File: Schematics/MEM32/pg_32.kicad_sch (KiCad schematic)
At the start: 16 parts

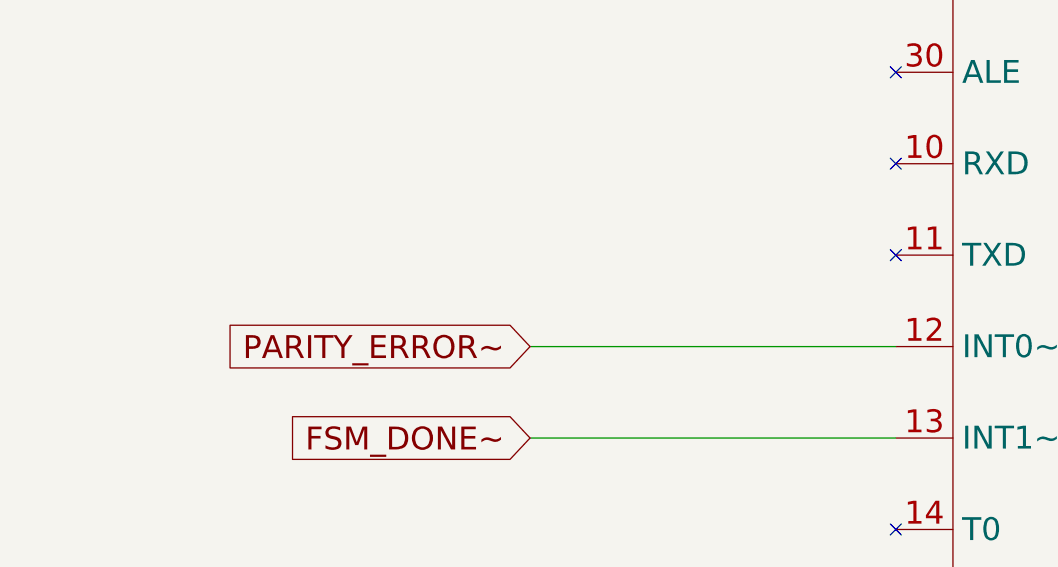
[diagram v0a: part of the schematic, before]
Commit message: MEM32: Disable parity check, good to 7.37s (rm096)
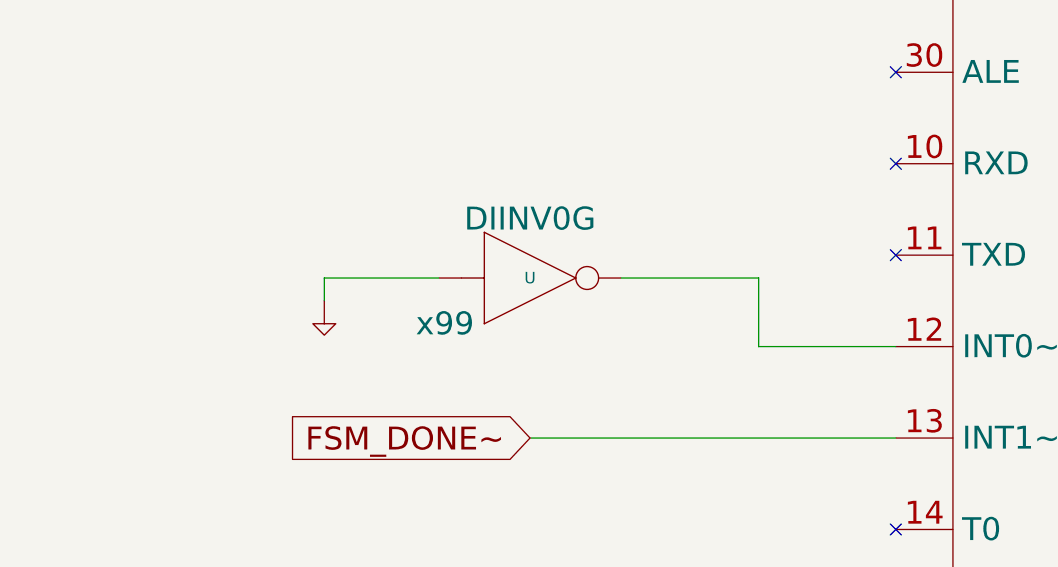
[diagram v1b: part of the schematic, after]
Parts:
- added U: (no value), symbol r1000:F04
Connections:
- net PD: now also U.1 (D0)
- net PARITY_ERROR~: no longer names the net of U.12 (INT0~)
- net PARITY_ERROR~: now also U.2 (Q)
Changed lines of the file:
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@@
-    (stroke (width 0) (type default))
-  )
-  (wire (pts (xy 88.9 137.16) (xy 129.54 137.16))
     (stroke (width 0) (type default))
   )
@@
     (stroke (width 0) (type default))
   )
+  (wire (pts (xy 66.04 129.54) (xy 78.74 129.54))
+    (stroke (width 0) (type default))
+  )
   (wire (pts (xy 289.56 243.84) (xy 289.56 248.92))
     (stroke (width 0) (type default))
@@
     (stroke (width 0) (type default))
   )
+  (wire (pts (xy 114.3 137.16) (xy 129.54 137.16))
+    (stroke (width 0) (type default))
+  )
   (wire (pts (xy 378.46 246.38) (xy 419.1 246.38))
     (stroke (width 0) (type default))
@@
     (stroke (width 0) (type default))
   )
+  (wire (pts (xy 114.3 129.54) (xy 114.3 137.16))
+    (stroke (width 0) (type default))
+  )
   (wire (pts (xy 289.56 233.68) (xy 292.1 233.68))
     (stroke (width 0) (type default))
@@
     (stroke (width 0) (type default))
   )
+  (wire (pts (xy 99.06 129.54) (xy 114.3 129.54))
+    (stroke (width 0) (type default))
+  )
   (wire (pts (xy 177.8 147.32) (xy 218.44 147.32))
     (stroke (width 0) (type default))
@@
     (stroke (width 0) (type default))
   )
+  (wire (pts (xy 66.04 132.08) (xy 66.04 129.54))
+    (stroke (width 0) (type default))
+  )
   (wire (pts (xy 523.24 160.02) (xy 535.94 160.02))
     (stroke (width 0) (type default))
@@
   (label "DIAG_4" (at 378.46 210.82 0) (fields_autoplaced)
     (effects (font (size 2.54 2.54)) (justify left bottom))
-  )
-  (global_label "PARITY_ERROR~" (shape input) (at 88.9 137.16 180) (fields_autoplaced)
-    (effects (font (size 2.54 2.54)) (justify right))
-    (property "Intersheet References" "${INTERSHEET_REFS}" (id 0) (at 55.3569 137.0013 0)
-      (effects (font (size 1.905 1.905)) (justify right))
-    )
   )
   (global_label "P_TO_S_SEL1" (shape input) (at 287.02 335.28 180) (fields_autoplaced)
@@
     (pin "2")
     (pin "3")
+  )
+  (symbol (lib_id "r1000:PD") (at 66.04 132.08 0) (unit 1)
+    (in_bom no) (on_board yes)
+    (default_instance (reference "U") (unit 1) (value "") (footprint ""))
+    (property "Reference" "U" (id 0) (at 66.04 132.08 0)
+      (effects (font (size 1.27 1.27)) hide)
+    )
+    (property "Value" "" (id 1) (at 66.04 132.08 0)
+      (effects (font (size 1.27 1.27)) hide)
+    )
+    (property "Footprint" "" (id 2) (at 66.04 132.08 0)
+      (effects (font (size 1.27 1.27)) hide)
+    )
+    (property "Datasheet" "" (id 3) (at 66.04 132.08 0)
+      (effects (font (size 1.27 1.27)) hide)
+    )
+    (pin "1")
   )
   (symbol (lib_id "r1000:F04") (at 513.08 160.02 0) (unit 1)
@@
     (pin "9")
   )
+  (symbol (lib_id "r1000:F04") (at 88.9 129.54 0) (unit 1)
+    (in_bom yes) (on_board yes)
+    (default_instance (reference "U") (unit 1) (value "") (footprint ""))
+    (property "Reference" "U" (id 0) (at 88.9 129.54 0)
+      (effects (font (size 1.27 1.27)))
+    )
+    (property "Value" "" (id 1) (at 90.17 134.62 0)
+      (effects (font (size 2.54 2.54)) (justify left))
+    )
+    (property "Footprint" "" (id 2) (at 88.9 129.54 0)
+      (effects (font (size 1.27 1.27)) hide)
+    )
+    (property "Datasheet" "" (id 3) (at 88.9 129.54 0)
+      (effects (font (size 1.27 1.27)) hide)
+    )
+    (property "Location" "x99" (id 4) (at 76.2 134.62 0)
+      (effects (font (size 2.54 2.54)) (justify left))
+    )
+    (property "Name" "DIINV0G" (id 5) (at 88.9 124.46 0)
+      (effects (font (size 2.54 2.54)) (justify bottom))
+    )
+    (pin "1")
+    (pin "2")
+  )
   (symbol (lib_id "r1000:NOVRAM") (at 213.36 350.52 0) (unit 1)

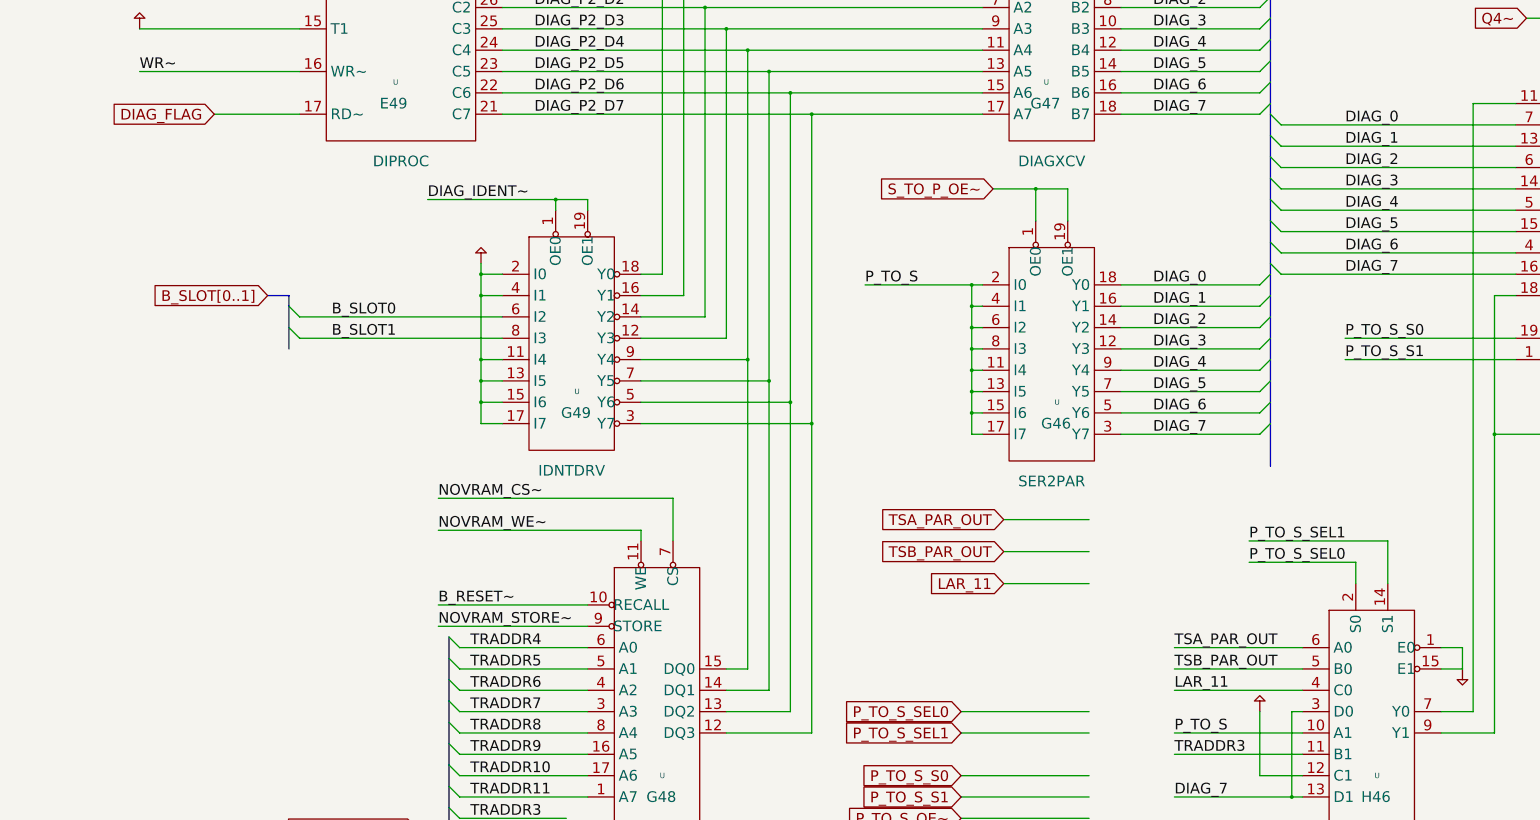
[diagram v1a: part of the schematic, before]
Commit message: DFSM pruning.  Tested to 13.72s
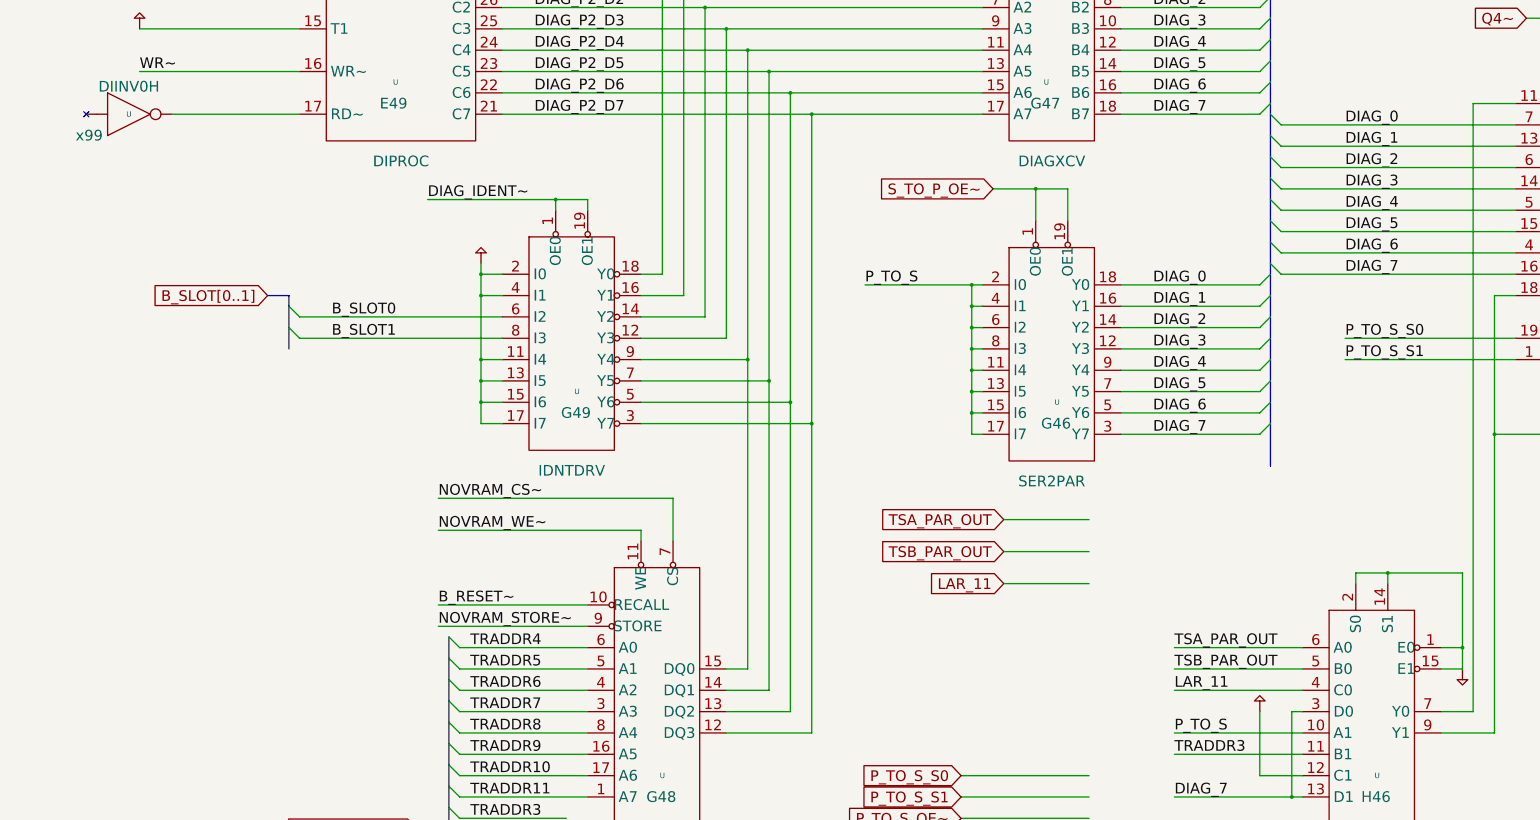
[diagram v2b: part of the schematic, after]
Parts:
- added U: (no value), symbol r1000:F04
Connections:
- net P_TO_S_SEL0 is gone; now on net PD: U.2 (S0)
- net P_TO_S_SEL1 is gone; now on net PD: U.14 (S1)
- net DIAG_FLAG: no longer names the net of U.17 (RD~)
- net DIAG_FLAG: now also U.2 (Q)
- no-connect marks 11 -> 12
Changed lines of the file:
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@@
   (junction (at 289.56 233.68) (diameter 0) (color 0 0 0 0)
   )
+  (junction (at 388.62 297.18) (diameter 0) (color 0 0 0 0)
+  )
   (junction (at 246.38 182.88) (diameter 0) (color 0 0 0 0)
   )
@@
   )
   (junction (at 289.56 254) (diameter 0) (color 0 0 0 0)
+  )
+  (junction (at 406.4 314.96) (diameter 0) (color 0 0 0 0)
   )
   (junction (at 289.56 248.92) (diameter 0) (color 0 0 0 0)
@@
   (no_connect (at 129.54 157.48))
   (no_connect (at 129.54 106.68))
+  (no_connect (at 78.74 187.96))
   (no_connect (at 129.54 116.84))
   (no_connect (at 129.54 127))
@@
     (stroke (width 0) (type default))
   )
-  (wire (pts (xy 355.6 294.64) (xy 381 294.64))
-    (stroke (width 0) (type default))
-  )
   (bus (pts (xy 294.64 83.82) (xy 294.64 88.9))
     (stroke (width 0) (type default))
@@
     (stroke (width 0) (type default))
   )
+  (wire (pts (xy 406.4 297.18) (xy 406.4 314.96))
+    (stroke (width 0) (type default))
+  )
   (wire (pts (xy 297.18 299.72) (xy 317.5 299.72))
     (stroke (width 0) (type default))
@@
     (stroke (width 0) (type default))
   )
+  (wire (pts (xy 381 297.18) (xy 388.62 297.18))
+    (stroke (width 0) (type default))
+  )
   (wire (pts (xy 325.12 233.68) (xy 358.14 233.68))
     (stroke (width 0) (type default))
@@
     (stroke (width 0) (type default))
   )
-  (wire (pts (xy 388.62 299.72) (xy 388.62 289.56))
-    (stroke (width 0) (type default))
-  )
   (wire (pts (xy 259.08 81.28) (xy 292.1 81.28))
     (stroke (width 0) (type default))
@@
     (stroke (width 0) (type default))
   )
-  (wire (pts (xy 287.02 335.28) (xy 317.5 335.28))
-    (stroke (width 0) (type default))
-  )
   (bus (pts (xy 360.68 203.2) (xy 360.68 208.28))
     (stroke (width 0) (type default))
@@
     (stroke (width 0) (type default))
   )
+  (wire (pts (xy 388.62 297.18) (xy 406.4 297.18))
+    (stroke (width 0) (type default))
+  )
   (wire (pts (xy 162.56 287.02) (xy 210.82 287.02))
     (stroke (width 0) (type default))
@@
     (stroke (width 0) (type default))
   )
+  (wire (pts (xy 388.62 299.72) (xy 388.62 297.18))
+    (stroke (width 0) (type default))
+  )
   (bus (pts (xy 360.68 226.06) (xy 360.68 231.14))
     (stroke (width 0) (type default))
   )
-  (wire (pts (xy 287.02 330.2) (xy 317.5 330.2))
-    (stroke (width 0) (type default))
-  )
   (wire (pts (xy 251.46 187.96) (xy 292.1 187.96))
     (stroke (width 0) (type default))
@@
     (stroke (width 0) (type default))
   )
+  (wire (pts (xy 381 299.72) (xy 381 297.18))
+    (stroke (width 0) (type default))
+  )
   (bus (pts (xy 360.68 185.42) (xy 360.68 187.96))
     (stroke (width 0) (type default))
@@
     (stroke (width 0) (type default))
   )
+  (wire (pts (xy 99.06 187.96) (xy 129.54 187.96))
+    (stroke (width 0) (type default))
+  )
   (wire (pts (xy 177.8 147.32) (xy 218.44 147.32))
     (stroke (width 0) (type default))
@@
     (stroke (width 0) (type default))
   )
-  (wire (pts (xy 109.22 187.96) (xy 129.54 187.96))
-    (stroke (width 0) (type default))
-  )
   (wire (pts (xy 210.82 231.14) (xy 220.98 231.14))
     (stroke (width 0) (type default))
@@
     (stroke (width 0) (type default))
   )
-  (wire (pts (xy 381 299.72) (xy 381 294.64))
-    (stroke (width 0) (type default))
-  )
   (wire (pts (xy 167.64 345.44) (xy 198.12 345.44))
     (stroke (width 0) (type default))
@@
     (stroke (width 0) (type default))
   )
-  (wire (pts (xy 355.6 289.56) (xy 388.62 289.56))
-    (stroke (width 0) (type default))
-  )
   (bus (pts (xy 360.68 165.1) (xy 360.68 170.18))
     (stroke (width 0) (type default))
@@
     (effects (font (size 2.54 2.54)) (justify left bottom))
   )
-  (label "P_TO_S_SEL0" (at 355.6 294.64 0) (fields_autoplaced)
-    (effects (font (size 2.54 2.54)) (justify left bottom))
-  )
   (label "TRADDR3" (at 170.18 355.6 0) (fields_autoplaced)
     (effects (font (size 2.54 2.54)) (justify left bottom))
@@
     (effects (font (size 2.54 2.54)) (justify left bottom))
   )
-  (label "P_TO_S_SEL1" (at 355.6 289.56 0) (fields_autoplaced)
-    (effects (font (size 2.54 2.54)) (justify left bottom))
-  )
   (label "DIAG_IDENT~" (at 185.42 132.08 0) (fields_autoplaced)
     (effects (font (size 2.54 2.54)) (justify left bottom))
@@
   (label "DIAG_4" (at 378.46 210.82 0) (fields_autoplaced)
     (effects (font (size 2.54 2.54)) (justify left bottom))
-  )
-  (global_label "P_TO_S_SEL1" (shape input) (at 287.02 335.28 180) (fields_autoplaced)
-    (effects (font (size 2.54 2.54)) (justify right))
-    (property "Intersheet References" "${INTERSHEET_REFS}" (id 0) (at 257.8312 335.1213 0)
-      (effects (font (size 1.905 1.905)) (justify right))
-    )
   )
   (global_label "TSA_PAR_OUT" (shape input) (at 297.18 284.48 180) (fields_autoplaced)
@@
     )
   )
-  (global_label "P_TO_S_SEL0" (shape input) (at 287.02 330.2 180) (fields_autoplaced)
-    (effects (font (size 2.54 2.54)) (justify right))
-    (property "Intersheet References" "${INTERSHEET_REFS}" (id 0) (at 257.8312 330.0413 0)
-      (effects (font (size 1.905 1.905)) (justify right))
-    )
-  )
   (global_label "DIAG_XCVR_OE~" (shape input) (at 302.26 127 180) (fields_autoplaced)
     (effects (font (size 2.54 2.54)) (justify right))
     (property "Intersheet References" "${INTERSHEET_REFS}" (id 0) (at 268.8378 126.8413 0)
-      (effects (font (size 1.905 1.905)) (justify right))
-    )
-  )
-  (global_label "DIAG_FLAG" (shape input) (at 109.22 187.96 180) (fields_autoplaced)
-    (effects (font (size 2.54 2.54)) (justify right))
-    (property "Intersheet References" "${INTERSHEET_REFS}" (id 0) (at 85.2321 187.8013 0)
       (effects (font (size 1.905 1.905)) (justify right))
     )
@@
     (pin "1")
   )
+  (symbol (lib_id "r1000:F04") (at 88.9 187.96 0) (unit 1)
+    (in_bom yes) (on_board yes)
+    (default_instance (reference "U") (unit 1) (value "") (footprint ""))
+    (property "Reference" "U" (id 0) (at 88.9 187.96 0)
+      (effects (font (size 1.27 1.27)))
+    )
+    (property "Value" "" (id 1) (at 90.17 193.04 0)
+      (effects (font (size 2.54 2.54)) (justify left))
+    )
+    (property "Footprint" "" (id 2) (at 88.9 187.96 0)
+      (effects (font (size 1.27 1.27)) hide)
+    )
+    (property "Datasheet" "" (id 3) (at 88.9 187.96 0)
+      (effects (font (size 1.27 1.27)) hide)
+    )
+    (property "Location" "x99" (id 4) (at 76.2 193.04 0)
+      (effects (font (size 2.54 2.54)) (justify left))
+    )
+    (property "Name" "DIINV0H" (id 5) (at 88.9 182.88 0)
+      (effects (font (size 2.54 2.54)) (justify bottom))
+    )
+    (pin "1")
+    (pin "2")
+  )
   (symbol (lib_id "r1000:F299") (at 434.34 246.38 0) (unit 1)
